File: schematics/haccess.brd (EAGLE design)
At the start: 86 x 86 mm, 34 parts, among them Q1 BSS123, SW1 SPST_TACT, SW2 SPST_TACT, U1 MCP2300X/SO, U2 ESP826607B, U3 OPTOISOLATOR-2SOIC8

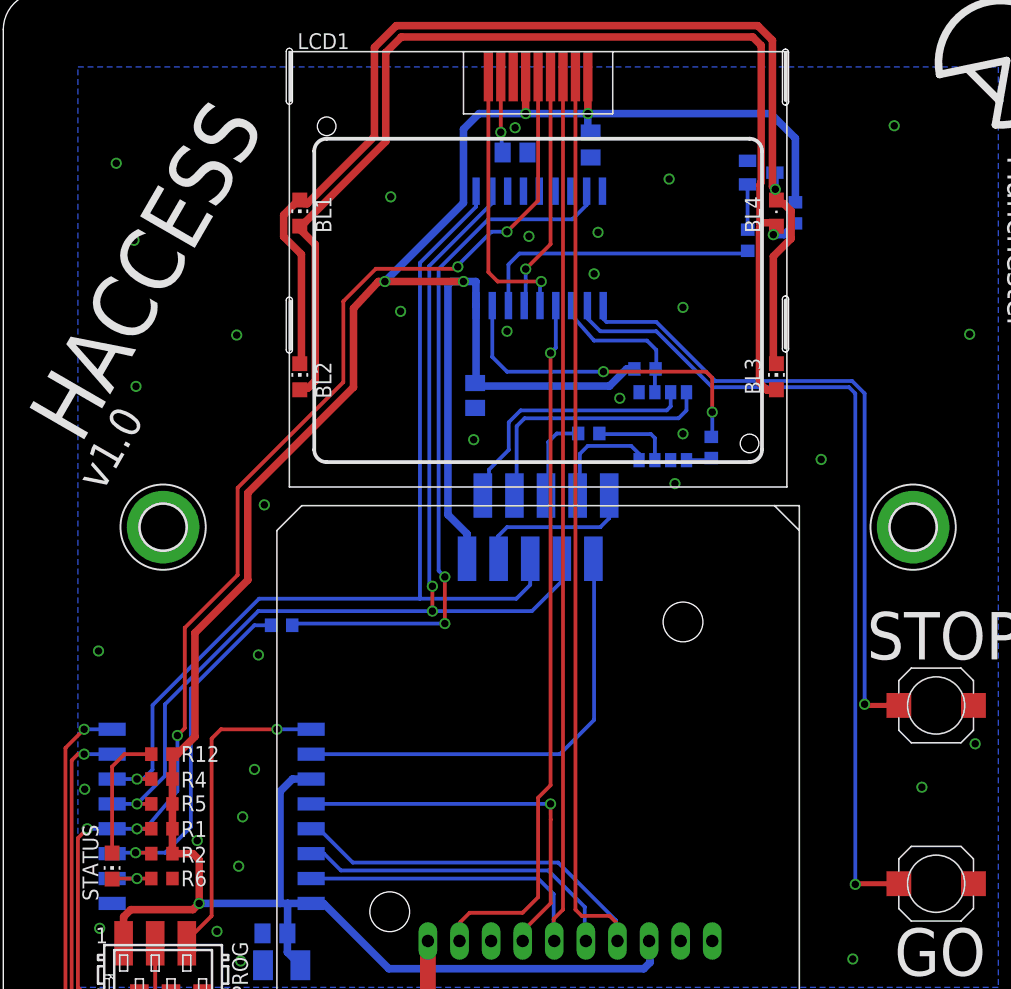
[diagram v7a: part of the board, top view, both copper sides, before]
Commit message: Moved Status LED onto pin expander, i2c and LCD reset pins onto pin 15
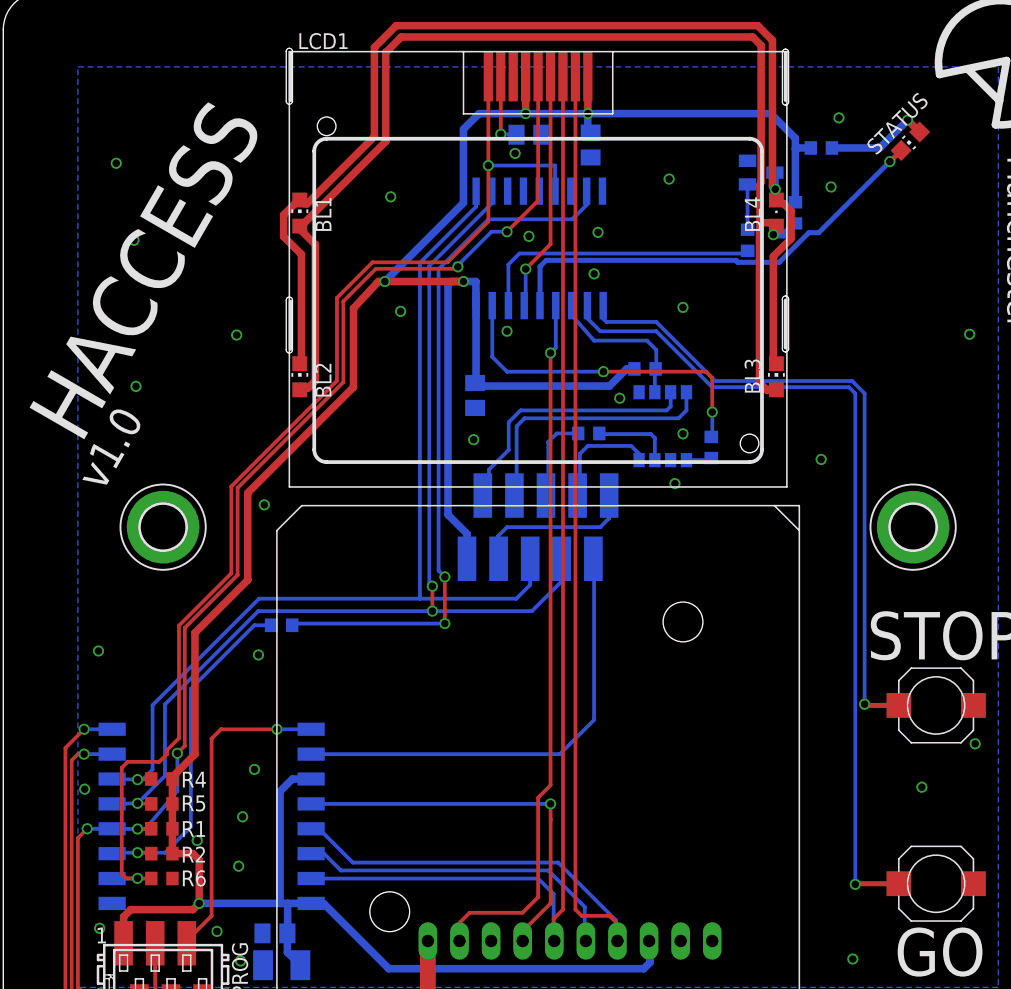
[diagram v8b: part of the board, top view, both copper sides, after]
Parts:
- moved STATUS 86.7 mm to (72.9, 74.0), turned to 135 degrees
- moved R12 72.0 mm to (65.8, 73.5), flipped to the bottom
- moved C1 1.81 mm to (42.3, 74.6)
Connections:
- removed net !RST: U1.6
- net !OUT_RESET_PERIPH: now also R6.2, U1.6, U2.GPIO15; no longer U1.14
- net OUT_STATUS_LED: now also U1.14; no longer R6.2, U2.GPIO15
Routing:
- net !OUT_RESET_PERIPH: track 22.3 -> 93.7 mm, vias 1 -> 2
- net OUT_STATUS_LED: track 5.17 -> 36.2 mm
- net N$2: track 10.5 -> 8.37 mm, vias 0 -> 1
- net +3V3: track 234.4 -> 235.5 mm
- net GND: vias 34 -> 35
